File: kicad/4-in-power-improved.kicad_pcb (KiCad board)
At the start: 2 copper layers, 84.1 x 61.7 mm, 189 parts, among them J1 USB_C_Receptacle_USB2.0_16P, J2 Bus_PCI_Express_x1, J3 Conn_01x02, Q1 FMMT493, Q2 AO3400A, Q3 AO3400A, U1 XC6206P332MR, U10 BQ25672RQMR, U11 TPS54331DR, U12 6.8uH, U13 TPS54331DR, U14 6.8uH, U15 6.8uH, U16 SX1308, U2 2P SMD 2.54P Jumper, U3 W25Q128JVP, U4 2P SMD 2.54P Jumper, U5 MCP25625T-E/ML, U6 RP2040, U7 S5B-XH-A(LF)(SN), U8 XT30PW-M, U9 BQ7694202PFBR, X1 ABM8-272-T3, Y1 X322516MLB4SI

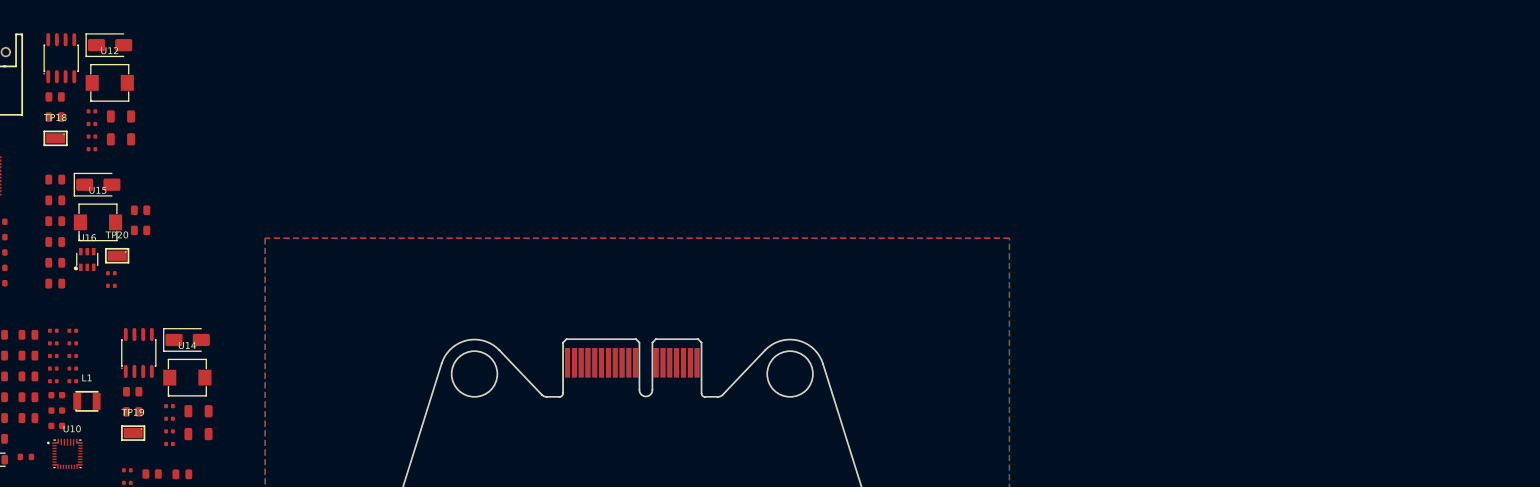
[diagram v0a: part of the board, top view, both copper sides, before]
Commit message: Bucks assigned to nicholas
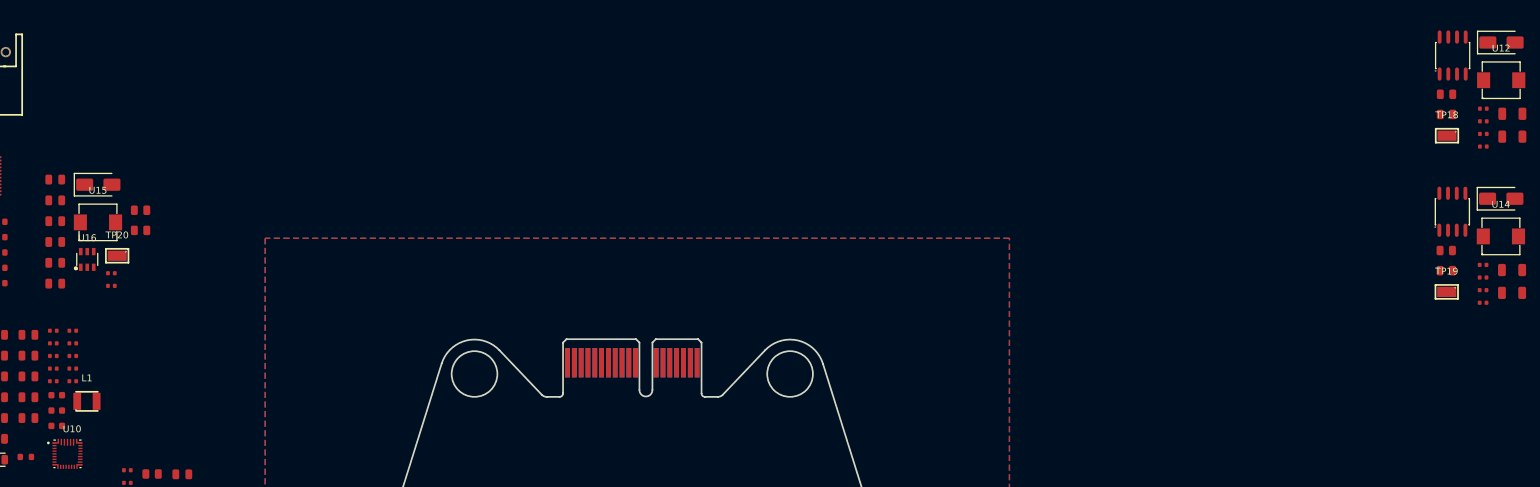
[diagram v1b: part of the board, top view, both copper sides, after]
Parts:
- moved C58 204.0 mm to (271.2, 26.9)
- moved C59 204.0 mm to (271.2, 28.8)
- moved C60 204.0 mm to (271.2, 30.6)
- moved C61 204.0 mm to (271.2, 32.5)
- moved C62 204.0 mm to (275.4, 27.6)
- moved C63 204.0 mm to (275.4, 31.0)
- moved TP18 204.0 mm to (265.8, 30.9)
- moved U11 204.0 mm to (266.7, 19.1)
- moved U12 204.0 mm to (273.8, 22.7)
- moved D14 204.0 mm to (273.8, 17.2)
- moved R45 204.0 mm to (265.8, 24.8)
- moved R46 204.0 mm to (265.8, 27.7)
- moved C64 193.7 mm to (271.1, 49.8)
- moved C65 193.7 mm to (271.1, 51.6)
- moved C66 193.7 mm to (271.1, 53.5)
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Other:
- board text added: "DO LAYOUT FOR THESE BUCKS. 4Layers. Make as compact as possible"
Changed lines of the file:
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@@
 	(footprint "PCM_JLCPCB:D_SMA"
 		(layer "F.Cu")
-		(at 69.86 17.59)
+		(at 273.83 17.2)
 		(descr "Diode SMA (DO-214AC)")
 		(tags "Diode SMA (DO-214AC)")
@@
 	(footprint "PCM_JLCPCB:SOIC-8_L5.0-W4.0-P1.27-LS6.0-BL"
 		(layer "F.Cu")
-		(at 62.7 19.5)
+		(at 266.67 19.11)
 		(descr "SOIC-8_L5.0-W4.0-P1.27-LS6.0-BL footprint")
 		(tags "SOIC-8_L5.0-W4.0-P1.27-LS6.0-BL footprint C7881")
@@
 	(footprint "4in-power:IND-SMD_L5.4-W5.2_SLO0530H6R8MTT"
 		(layer "F.Cu")
-		(at 69.815005 23.1174)
+		(at 273.785005 22.7274)
 		(descr "IND-SMD_L5.4-W5.2_SLO0530H6R8MTT footprint")
 		(tags "IND-SMD_L5.4-W5.2_SLO0530H6R8MTT footprint C325965")
@@
 	(footprint "PCM_JLCPCB:C_0402"
 		(layer "F.Cu")
-		(at 78.57 74.2)
+		(at 271.13 53.5)
 		(descr "Capacitor SMD 0402 (1005 Metric), square (rectangular) end terminal, IPC_7351 nominal, (Body size source: IPC-SM-782 page 76, https://www.pcb-3d.com/wordpress/wp-content/uploads/ipc-sm-782a_amendment_1_and_2.pdf), generated with kicad-footprint-generator")
 		(tags "capacitor")
@@
 	(footprint "4in-power:SMD_RH-5015"
 		(layer "F.Cu")
-		(at 61.873003 31.248002)
+		(at 265.843003 30.858002)
 		(descr "SMD_RH-5015 footprint")
 		(tags "SMD_RH-5015 footprint C5199798")
@@
 	(footprint "4in-power:SMD_RH-5015"
 		(layer "F.Cu")
-		(at 73.243003 74.458002)
+		(at 265.803003 53.758002)
 		(descr "SMD_RH-5015 footprint")
 		(tags "SMD_RH-5015 footprint C5199798")
@@
 	(footprint "PCM_JLCPCB:R_0805"
 		(layer "F.Cu")
-		(at 73.17 71.34)
+		(at 265.73 50.64)
 		(descr "Resistor SMD 0805 (2012 Metric), square (rectangular) end terminal, IPC_7351 nominal, (Body size source: IPC-SM-782 page 72, https://www.pcb-3d.com/wordpress/wp-content/uploads/ipc-sm-782a_amendment_1_and_2.pdf), generated with kicad-footprint-generator")
 		(tags "resistor")
@@
 	(footprint "PCM_JLCPCB:C_0402"
 		(layer "F.Cu")
-		(at 67.2 27.29)
+		(at 271.17 26.9)
 		(descr "Capacitor SMD 0402 (1005 Metric), square (rectangular) end terminal, IPC_7351 nominal, (Body size source: IPC-SM-782 page 76, https://www.pcb-3d.com/wordpress/wp-content/uploads/ipc-sm-782a_amendment_1_and_2.pdf), generated with kicad-footprint-generator")
 		(tags "capacitor")
@@
 	(footprint "PCM_JLCPCB:R_0805"
 		(layer "F.Cu")
-		(at 61.8 25.18)
+		(at 265.77 24.79)
 		(descr "Resistor SMD 0805 (2012 Metric), square (rectangular) end terminal, IPC_7351 nominal, (Body size source: IPC-SM-782 page 72, https://www.pcb-3d.com/wordpress/wp-content/uploads/ipc-sm-782a_amendment_1_and_2.pdf), generated with kicad-footprint-generator")
 		(tags "resistor")
@@
 	(footprint "4in-power:IND-SMD_L5.4-W5.2_SLO0530H6R8MTT"
 		(layer "F.Cu")
-		(at 81.185005 66.3274)
+		(at 273.745005 45.6274)
 		(descr "IND-SMD_L5.4-W5.2_SLO0530H6R8MTT footprint")
 		(tags "IND-SMD_L5.4-W5.2_SLO0530H6R8MTT footprint C325965")
@@
 	(footprint "PCM_JLCPCB:C_1206"
 		(layer "F.Cu")
-		(at 82.82 71.25)
+		(at 275.38 50.55)
 		(descr "Capacitor SMD 1206 (3216 Metric), square (rectangular) end terminal, IPC_7351 nominal, (Body size source: IPC-SM-782 page 76, https://www.pcb-3d.com/wordpress/wp-content/uploads/ipc-sm-782a_amendment_1_and_2.pdf), generated with kicad-footprint-generator")
 		(tags "capacitor")
@@
 	(footprint "PCM_JLCPCB:C_0402"
 		(layer "F.Cu")
-		(at 67.2 30.99)
+		(at 271.17 30.6)
 		(descr "Capacitor SMD 0402 (1005 Metric), square (rectangular) end terminal, IPC_7351 nominal, (Body size source: IPC-SM-782 page 76, https://www.pcb-3d.com/wordpress/wp-content/uploads/ipc-sm-782a_amendment_1_and_2.pdf), generated with kicad-footprint-generator")
 		(tags "capacitor")
@@
 	(footprint "PCM_JLCPCB:R_0805"
 		(layer "F.Cu")
-		(at 73.17 68.39)
+		(at 265.73 47.69)
 		(descr "Resistor SMD 0805 (2012 Metric), square (rectangular) end terminal, IPC_7351 nominal, (Body size source: IPC-SM-782 page 72, https://www.pcb-3d.com/wordpress/wp-content/uploads/ipc-sm-782a_amendment_1_and_2.pdf), generated with kicad-footprint-generator")
 		(tags "resistor")
@@
 	(footprint "PCM_JLCPCB:C_1206"
 		(layer "F.Cu")
-		(at 71.45 28.04)
+		(at 275.42 27.65)
 		(descr "Capacitor SMD 1206 (3216 Metric), square (rectangular) end terminal, IPC_7351 nominal, (Body size source: IPC-SM-782 page 76, https://www.pcb-3d.com/wordpress/wp-content/uploads/ipc-sm-782a_amendment_1_and_2.pdf), generated with kicad-footprint-generator")
 		(tags "capacitor")
@@
 	(footprint "PCM_JLCPCB:C_0402"
 		(layer "F.Cu")
-		(at 78.57 76.05)
+		(at 271.13 55.35)
 		(descr "Capacitor SMD 0402 (1005 Metric), square (rectangular) end terminal, IPC_7351 nominal, (Body size source: IPC-SM-782 page 76, https://www.pcb-3d.com/wordpress/wp-content/uploads/ipc-sm-782a_amendment_1_and_2.pdf), generated with kicad-footprint-generator")
 		(tags "capacitor")
@@
 	(footprint "PCM_JLCPCB:C_0402"
 		(layer "F.Cu")
-		(at 67.2 29.14)
+		(at 271.17 28.75)
 		(descr "Capacitor SMD 0402 (1005 Metric), square (rectangular) end terminal, IPC_7351 nominal, (Body size source: IPC-SM-782 page 76, https://www.pcb-3d.com/wordpress/wp-content/uploads/ipc-sm-782a_amendment_1_and_2.pdf), generated with kicad-footprint-generator")
 		(tags "capacitor")
@@
 	(footprint "PCM_JLCPCB:C_1206"
 		(layer "F.Cu")
-		(at 82.82 74.6)
+		(at 275.38 53.9)
 		(descr "Capacitor SMD 1206 (3216 Metric), square (rectangular) end terminal, IPC_7351 nominal, (Body size source: IPC-SM-782 page 76, https://www.pcb-3d.com/wordpress/wp-content/uploads/ipc-sm-782a_amendment_1_and_2.pdf), generated with kicad-footprint-generator")
 		(tags "capacitor")
@@
 	(footprint "PCM_JLCPCB:R_0805"
 		(layer "F.Cu")
-		(at 61.8 28.13)
+		(at 265.77 27.74)
 		(descr "Resistor SMD 0805 (2012 Metric), square (rectangular) end terminal, IPC_7351 nominal, (Body size source: IPC-SM-782 page 72, https://www.pcb-3d.com/wordpress/wp-content/uploads/ipc-sm-782a_amendment_1_and_2.pdf), generated with kicad-footprint-generator")
 		(tags "resistor")
@@
 	(footprint "PCM_JLCPCB:D_SMA"
 		(layer "F.Cu")
-		(at 81.23 60.8)
+		(at 273.79 40.1)
 		(descr "Diode SMA (DO-214AC)")
 		(tags "Diode SMA (DO-214AC)")
@@
 	(footprint "PCM_JLCPCB:C_1206"
 		(layer "F.Cu")
-		(at 71.45 31.39)
+		(at 275.42 31)
 		(descr "Capacitor SMD 1206 (3216 Metric), square (rectangular) end terminal, IPC_7351 nominal, (Body size source: IPC-SM-782 page 76, https://www.pcb-3d.com/wordpress/wp-content/uploads/ipc-sm-782a_amendment_1_and_2.pdf), generated with kicad-footprint-generator")
 		(tags "capacitor")
@@
 	(footprint "PCM_JLCPCB:C_0402"
 		(layer "F.Cu")
-		(at 78.57 70.5)
+		(at 271.13 49.8)
 		(descr "Capacitor SMD 0402 (1005 Metric), square (rectangular) end terminal, IPC_7351 nominal, (Body size source: IPC-SM-782 page 76, https://www.pcb-3d.com/wordpress/wp-content/uploads/ipc-sm-782a_amendment_1_and_2.pdf), generated with kicad-footprint-generator")
 		(tags "capacitor")
@@
 	(footprint "PCM_JLCPCB:SOIC-8_L5.0-W4.0-P1.27-LS6.0-BL"
 		(layer "F.Cu")
-		(at 74.07 62.71)
+		(at 266.63 42.01)
 		(descr "SOIC-8_L5.0-W4.0-P1.27-LS6.0-BL footprint")
 		(tags "SOIC-8_L5.0-W4.0-P1.27-LS6.0-BL footprint C7881")
@@
 	(footprint "PCM_JLCPCB:C_0402"
 		(layer "F.Cu")
-		(at 67.2 32.84)
+		(at 271.17 32.45)
 		(descr "Capacitor SMD 0402 (1005 Metric), square (rectangular) end terminal, IPC_7351 nominal, (Body size source: IPC-SM-782 page 76, https://www.pcb-3d.com/wordpress/wp-content/uploads/ipc-sm-782a_amendment_1_and_2.pdf), generated with kicad-footprint-generator")
 		(tags "capacitor")
@@
 	(footprint "PCM_JLCPCB:C_0402"
 		(layer "F.Cu")
-		(at 78.57 72.35)
+		(at 271.13 51.65)
 		(descr "Capacitor SMD 0402 (1005 Metric), square (rectangular) end terminal, IPC_7351 nominal, (Body size source: IPC-SM-782 page 76, https://www.pcb-3d.com/wordpress/wp-content/uploads/ipc-sm-782a_amendment_1_and_2.pdf), generated with kicad-footprint-generator")
 		(tags "capacitor")
@@
 		(layer "Edge.Cuts")
 	)
+	(gr_text "DO LAYOUT FOR THESE BUCKS. 4Layers. Make as compact as possible"
+		(at 242.5 36.5 0)
+		(layer "User.1")
+		(effects
+			(font
+				(size 1 1)
+				(thickness 0.15)
+			)
+			(justify left bottom)
+		)
+	)
 	(zone

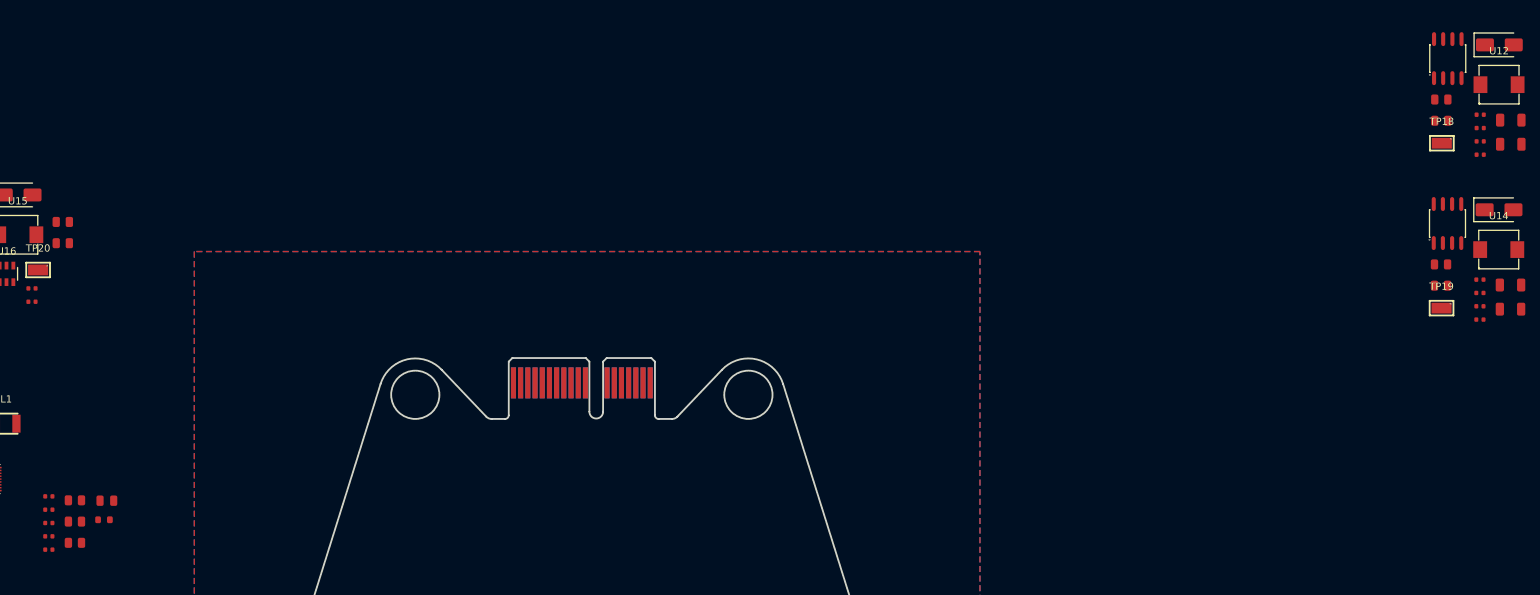
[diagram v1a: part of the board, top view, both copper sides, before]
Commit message: 3.3V and 5V buck regulator layout
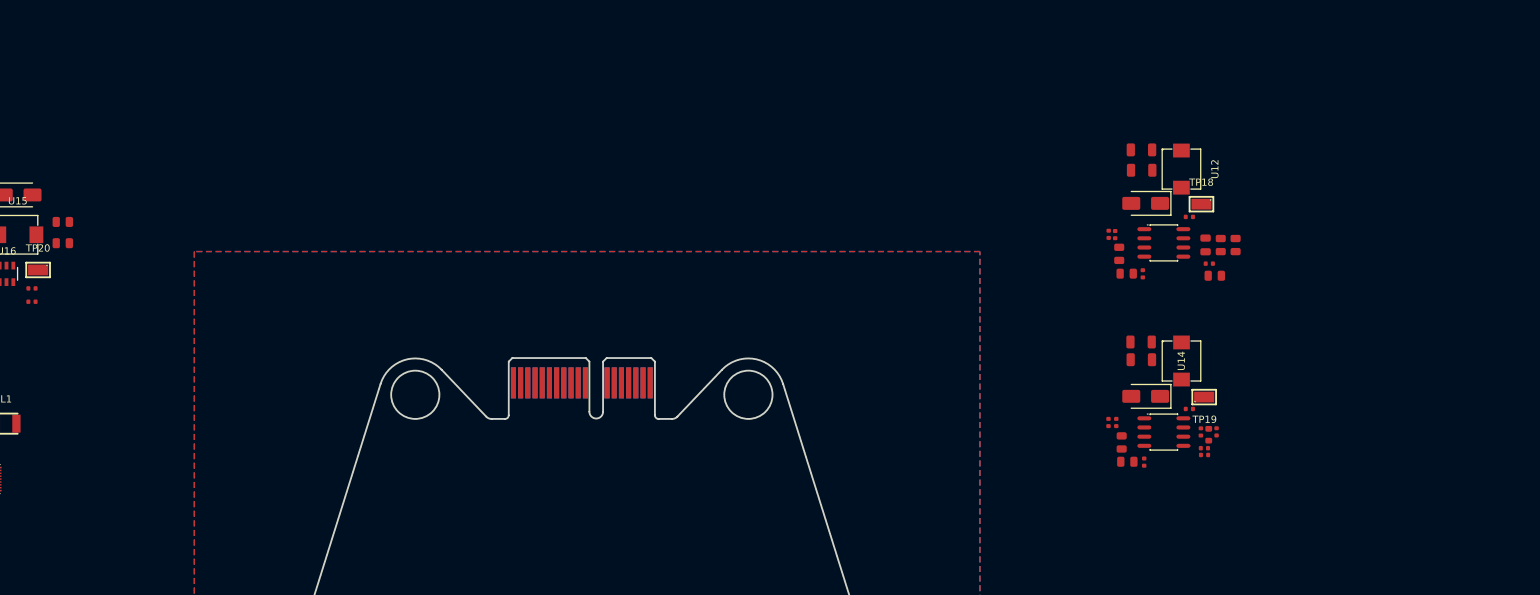
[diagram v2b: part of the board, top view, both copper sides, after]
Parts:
- moved R15 165.7 mm to (237.2, 45.0), turned to 90 degrees
- moved R16 164.4 mm to (235.1, 45.0), turned to 90 degrees
- moved C19 164.4 mm to (233.6, 47.6)
- moved R18 163.0 mm to (234.6, 70.9), turned to 90 degrees
- moved R14 161.3 mm to (234.3, 49.3), turned to 180 degrees
- moved R17 160.9 mm to (232.9, 74.2), turned to 180 degrees
- moved C21 160.7 mm to (232.9, 73.2)
- moved C22 160.5 mm to (232.4, 71.0), turned to 90 degrees
- moved C20 156.7 mm to (233.0, 45.0), turned to 90 degrees
- moved R19 153.9 mm to (233.5, 71.3), turned to 90 degrees
- moved D15 55.5 mm to (224.7, 66.0), turned to 180 degrees
- moved C65 54.6 mm to (219.6, 69.6), turned to 90 degrees
- moved C64 54.3 mm to (220.6, 69.6), turned to 90 degrees
- moved C58 54.2 mm to (219.6, 43.5), turned to 90 degrees
- moved D14 53.8 mm to (224.7, 39.2), turned to 180 degrees
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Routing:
- net /Power/StepDown3.3V/R2: track 0.00 -> 0.91 mm
